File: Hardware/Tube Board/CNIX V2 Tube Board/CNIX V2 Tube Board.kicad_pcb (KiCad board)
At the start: 2 copper layers, 185 x 51 mm, 50 parts, among them J1 VDD, J2 GND, J3 Tube Conn, J4 LED, J5 HT, U1 SN75468, U10 IN-4_0, U11 IN-4_1, U12 IN-4_2, U13 IN-4_3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

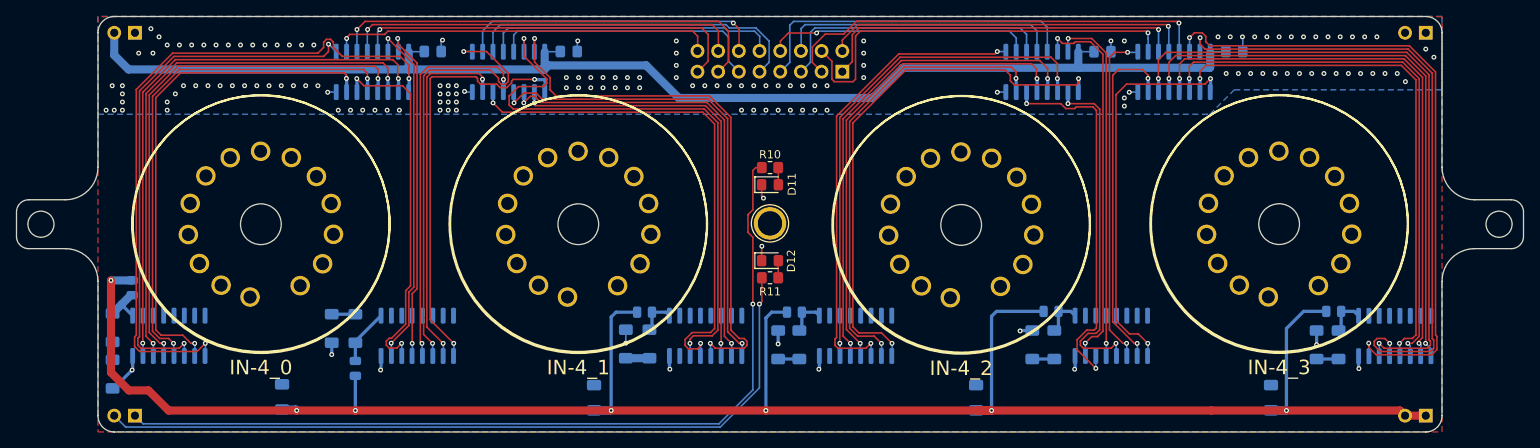
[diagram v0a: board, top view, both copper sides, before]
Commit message: finished wiring fix for the tube board
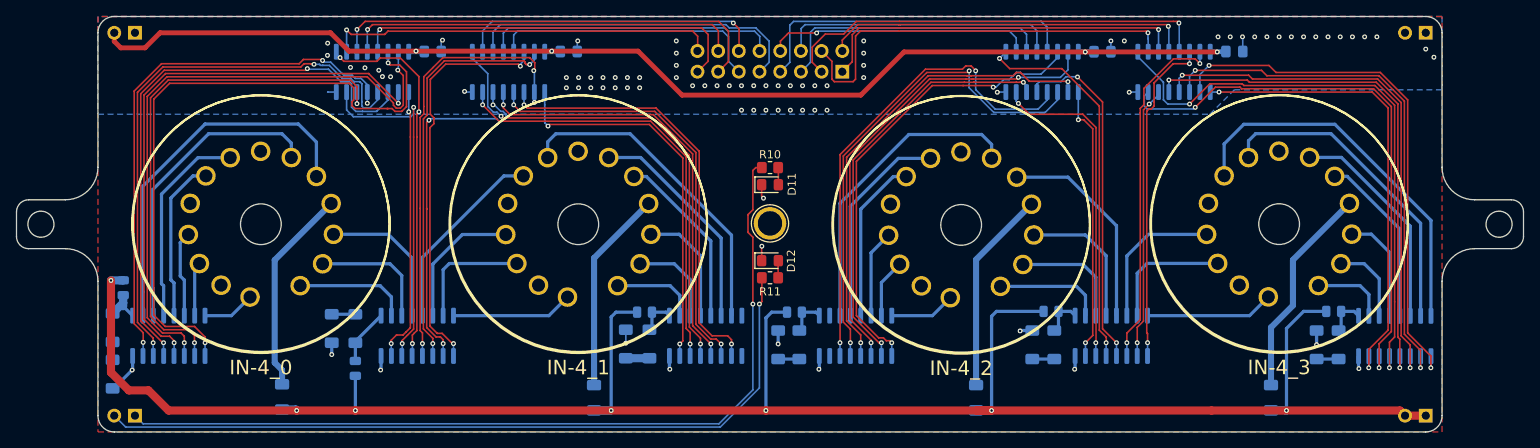
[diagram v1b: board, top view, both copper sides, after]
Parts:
- moved R12 1.10 mm to (69.1, 108.3)
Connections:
- U1 pad 1: /T1_D4 -> /T1_D1
- U1 pad 10: /T0_K1 -> /T0_K4
- U1 pad 11: /T0_K5 -> /T0_K6
- U1 pad 12: /T0_K3 -> /T0_K8
- U1 pad 13: /T1_K9 -> /T1_K2
- U1 pad 14: /T1_K8 -> /T1_K3
- U1 pad 15: /T1_K6 -> /T1_K5
- U1 pad 16: /T1_K4 -> /T1_K1
- U1 pad 2: /T1_D6 -> /T1_D5
- U1 pad 3: /T1_D8 -> /T1_D3
- U1 pad 4: /T1_D9 -> /T1_D2
- U1 pad 5: /T0_D3 -> /T0_D8
- U1 pad 6: /T0_D5 -> /T0_D6
- U1 pad 7: /T0_D1 -> /T0_D4
- U14 pad 1: /T0_D4 -> /T0_D1
- U14 pad 10: /T0_K2 -> /T0_K9
- U14 pad 11: /T0_K0 -> /T0_K7
- U14 pad 12: /T0_K7 -> /T0_K0
- U14 pad 13: /T0_K9 -> /T0_K2
- U14 pad 14: /T0_K8 -> /T0_K3
- U14 pad 15: /T0_K6 -> /T0_K5
- U14 pad 16: /T0_K4 -> /T0_K1
- U14 pad 2: /T0_D6 -> /T0_D5
- U14 pad 3: /T0_D8 -> /T0_D3
- U14 pad 4: /T0_D9 -> /T0_D2
- U14 pad 5: /T0_D7 -> /T0_D0
- U14 pad 6: /T0_D0 -> /T0_D7
- U14 pad 7: /T0_D2 -> /T0_D9
- U2 pad 1: /T1_D7 -> unconnected-(U2-I1-Pad1)
- U2 pad 10: unconnected-(U2-O7-Pad10) -> /T1_K4
- U2 pad 11: /T1_K1 -> /T1_K6
- U2 pad 12: /T1_K5 -> /T1_K8
- U2 pad 13: /T1_K3 -> /T1_K9
- U2 pad 14: /T1_K2 -> /T1_K7
- U2 pad 16: /T1_K7 -> unconnected-(U2-O1-Pad16)
- U2 pad 3: /T1_D2 -> /T1_D7
- U2 pad 4: /T1_D3 -> /T1_D9
- U2 pad 5: /T1_D5 -> /T1_D8
- U2 pad 6: /T1_D1 -> /T1_D6
- U2 pad 7: unconnected-(U2-I7-Pad7) -> /T1_D4
- U3 pad 1: /T2_D4 -> /T2_D1
- U3 pad 11: /T2_K0 -> /T2_K7
- U3 pad 12: /T2_K7 -> /T2_K0
- U3 pad 13: /T2_K9 -> /T2_K2
- U3 pad 14: /T2_K8 -> /T2_K3
- U3 pad 15: /T2_K6 -> /T2_K5
- U3 pad 16: /T2_K4 -> /T2_K1
- U3 pad 2: /T2_D6 -> /T2_D5
- U3 pad 3: /T2_D8 -> /T2_D3
- U3 pad 4: /T2_D9 -> /T2_D2
- U3 pad 5: /T2_D7 -> /T2_D0
- U3 pad 6: /T2_D0 -> /T2_D7
- U4 pad 1: /T3_D4 -> /T3_D1
- U4 pad 10: /T2_K1 -> /T2_K4
- U4 pad 11: /T2_K5 -> /T2_K6
- U4 pad 12: /T2_K3 -> /T2_K8
- U4 pad 13: /T2_K2 -> /T2_K9
- U4 pad 14: /T3_K8 -> /T3_K3
- U4 pad 15: /T3_K6 -> /T3_K5
- U4 pad 16: /T3_K4 -> /T3_K1
- U4 pad 2: /T3_D6 -> /T3_D5
- U4 pad 3: /T3_D8 -> /T3_D3
- U4 pad 4: /T2_D2 -> /T2_D9
- U4 pad 5: /T2_D3 -> /T2_D8
- U4 pad 6: /T2_D5 -> /T2_D6
- U4 pad 7: /T2_D1 -> /T2_D4
- U5 pad 1: /T3_D9 -> /T3_D2
- U5 pad 10: /T3_K1 -> /T3_K4
- U5 pad 11: /T3_K5 -> /T3_K6
- U5 pad 12: /T3_K3 -> /T3_K8
- U5 pad 13: /T3_K2 -> /T3_K9
- U5 pad 14: /T3_K0 -> /T3_K7
- U5 pad 15: /T3_K7 -> /T3_K0
- U5 pad 16: /T3_K9 -> /T3_K2
- U5 pad 2: /T3_D7 -> /T3_D0
- U5 pad 3: /T3_D0 -> /T3_D7
- U5 pad 4: /T3_D2 -> /T3_D9
- U5 pad 5: /T3_D3 -> /T3_D8
- U5 pad 6: /T3_D5 -> /T3_D6
- U5 pad 7: /T3_D1 -> /T3_D4
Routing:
- net /T0_D4: track 84.0 -> 33.9 mm
- net /T3_K2: track 0.00 -> 46.9 mm
- net /T3_D5: track 80.3 -> 33.5 mm
- net /T0_K9: track 0.00 -> 45.5 mm
- net /T1_K0: track 0.00 -> 40.0 mm
- net /T3_K0: track 0.00 -> 39.5 mm
- net /T3_D1: track 79.8 -> 40.9 mm
- net /T2_K7: track 0.00 -> 38.1 mm
- net /T0_K7: track 0.00 -> 37.7 mm
- net /T0_D1: track 43.1 -> 79.8 mm
- net /T3_D3: track 78.5 -> 43.8 mm
- net /T0_D3: track 41.9 -> 76.3 mm
- net /T2_D4: track 66.1 -> 33.9 mm
- net /T3_D8: track 41.6 -> 71.8 mm
- net /T1_K7: track 0.00 -> 27.4 mm
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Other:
- board text removed: "FAIL: Tuibes are wired backwards, needs fixing"

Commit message: finished tube PCB IN4 Version
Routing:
- net /T1_D4: track 47.1 -> 62.6 mm
- net GND: track 35.0 -> 31.4 mm, vias 85 -> 218
- net /T0_D9: track 66.8 -> 65.4 mm, vias 3 -> 2
- net /T1_D2: track 54.4 -> 53.1 mm, vias 3 -> 2
- net /T1_D5: track 44.3 -> 44.1 mm, vias 3 -> 2
- net /T0_D8: vias 3 -> 2
